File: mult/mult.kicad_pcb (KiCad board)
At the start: 2 copper layers, 20 x 108 mm, 73 parts, among them J1 Eurorack_Power, J10 Eurorack_Mono_Jack, J11 Eurorack_Mono_Jack, J12 Eurorack_Mono_Jack_No_S, J13 Eurorack_Mono_Jack_No_S, J14 Eurorack_Mono_Jack, J15 Eurorack_Mono_Jack, J16 Eurorack_Mono_Jack_No_S, J17 Eurorack_Mono_Jack_No_S, J2 Eurorack_Mono_Jack, J3 Eurorack_Mono_Jack, J4 Eurorack_Mono_Jack_No_S, J5 Eurorack_Mono_Jack_No_S, J6 Eurorack_Mono_Jack, J7 Eurorack_Mono_Jack, J8 Eurorack_Mono_Jack_No_S, J9 Eurorack_Mono_Jack_No_S, U1 OPA4197xPW, U2 OPA4197xPW, U3 OPA4197xPW, U4 OPA4197xPW

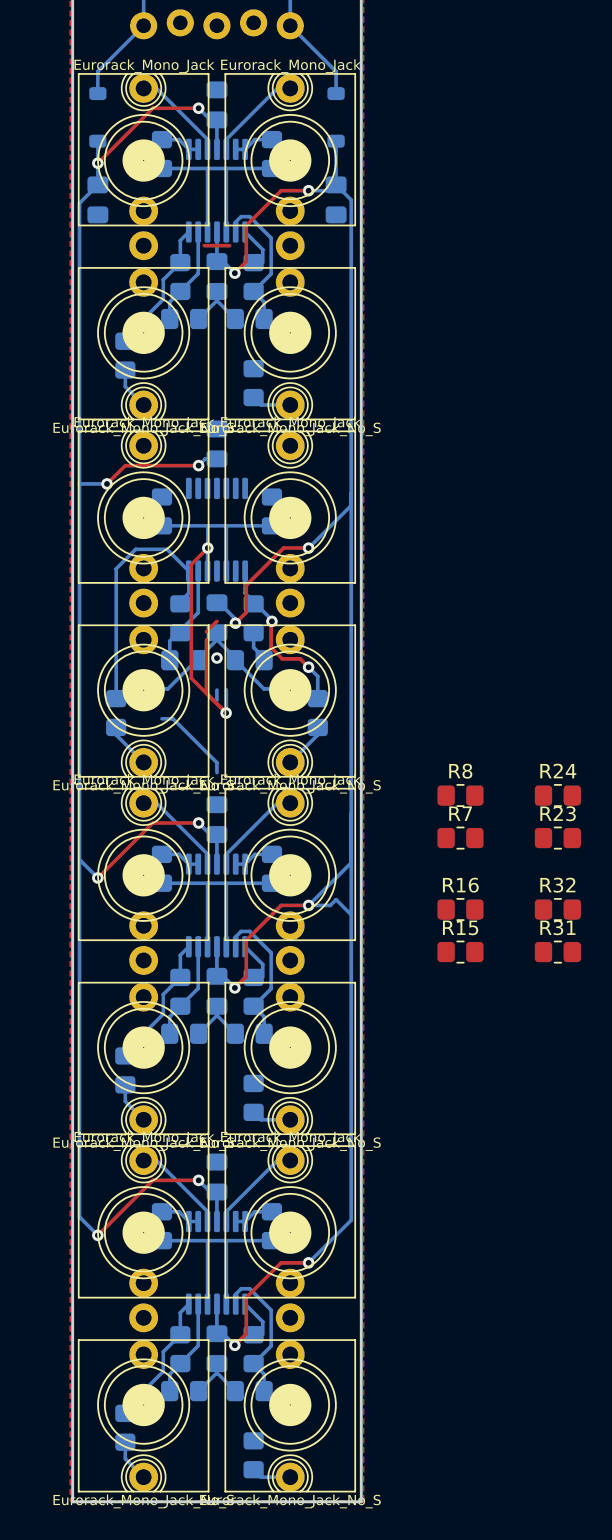
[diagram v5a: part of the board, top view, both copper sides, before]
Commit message: mult: Initial board routed, all items connected
Still expecting to make major changes this looks like mostly-random item
placements.
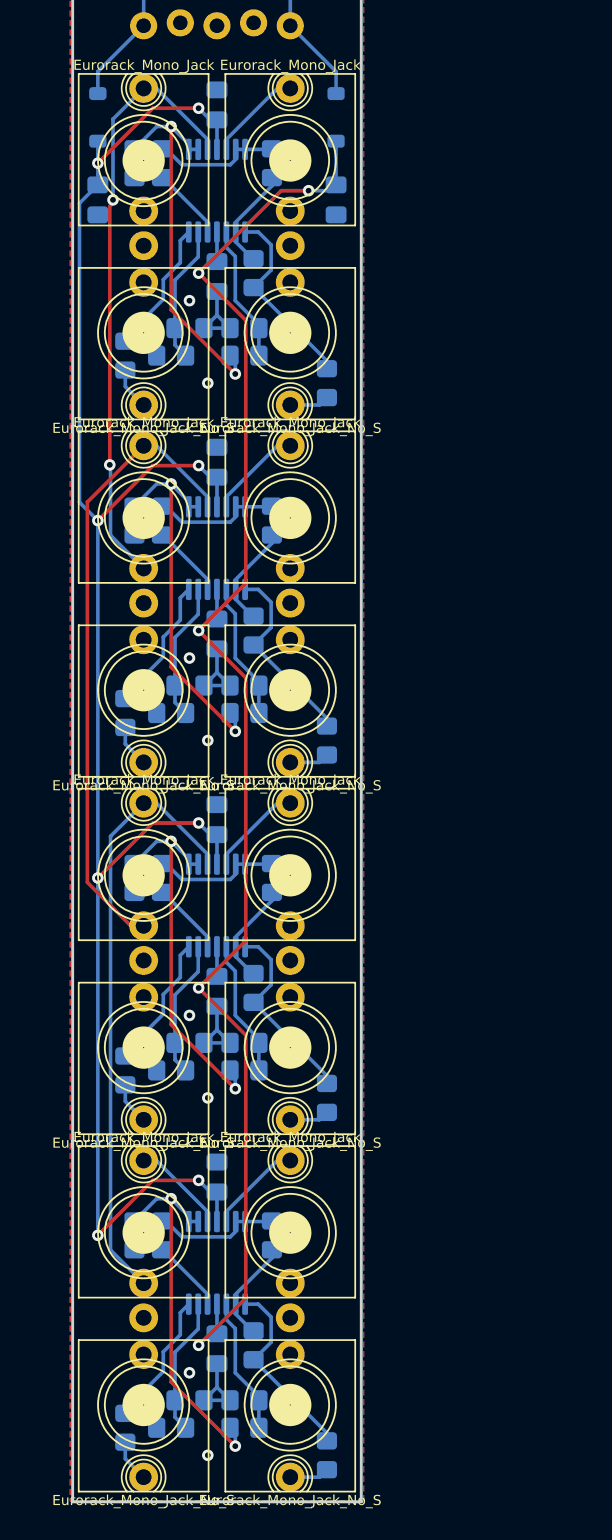
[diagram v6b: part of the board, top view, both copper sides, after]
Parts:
- R15, R16, R23, R24, R31, R32, R7, R8: moved to B.Cu
- moved R7 48.6 mm to (14.0, 15.2), turned to 90 degrees
- moved R8 38.9 mm to (12.7, 22.9), turned to -90 degrees
- moved R32 36.8 mm to (12.7, 97.2), turned to -90 degrees
- moved R15 32.6 mm to (14.0, 40.0), turned to 90 degrees
- moved R31 27.9 mm to (14.0, 89.5), turned to 90 degrees
- moved R24 24.9 mm to (12.7, 72.4), turned to -90 degrees
- moved R16 24.1 mm to (12.7, 47.6), turned to -90 degrees
- moved R23 20.0 mm to (14.0, 64.8), turned to 90 degrees
- moved R10 7.65 mm to (6.35, 40.0), turned to -90 degrees
- moved R18 7.65 mm to (6.35, 64.8), turned to -90 degrees
- moved R2 7.65 mm to (6.35, 15.2), turned to -90 degrees
- moved R26 7.65 mm to (6.35, 89.5), turned to -90 degrees
- moved R11 6.60 mm to (6.99, 53.3), turned to 180 degrees
- moved R13 6.60 mm to (12.1, 53.3), turned to 180 degrees
- moved R19 5.48 mm to (6.99, 78.1), turned to 180 degrees
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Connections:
- R13 pad 2: Net-(U2B--) -> Net-(U2A--)
- R15 pad 2: Net-(U2A--) -> Net-(U2B--)
- R21 pad 2: Net-(U3B--) -> Net-(U3A--)
- R23 pad 2: Net-(U3A--) -> Net-(U3B--)
- R29 pad 2: Net-(U4B--) -> Net-(U4A--)
- R31 pad 2: Net-(U4A--) -> Net-(U4B--)
- R5 pad 2: Net-(U1B--) -> Net-(U1A--)
- R7 pad 2: Net-(U1A--) -> Net-(U1B--)
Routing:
- net (no net): track 86.1 -> 0.00 mm
- net /channel 2/tip in (a): track 0.00 -> 43.6 mm
- net VEE: track 149.0 -> 109.0 mm, vias 8 -> 5
- net /channel 1/tip in (a): track 6.58 -> 42.1 mm, vias 0 -> 2
- net /channel 3/tip in (a): track 6.58 -> 41.8 mm
- net Net-(U2A--): track 0.00 -> 25.5 mm, vias 0 -> 2
- net Net-(U3A--): track 2.79 -> 25.5 mm, vias 0 -> 2
- net Net-(U1A--): track 2.79 -> 25.5 mm, vias 0 -> 2
- net Net-(U4A--): track 2.79 -> 25.5 mm, vias 0 -> 2
- net Net-(R32-Pad2): track 0.00 -> 13.4 mm
- net Net-(R24-Pad2): track 0.00 -> 13.4 mm
- net Net-(R34-Pad1): track 0.00 -> 13.4 mm
- net Net-(R16-Pad2): track 0.00 -> 13.4 mm
- net Net-(U3C-+): track 0.00 -> 9.23 mm
- net Net-(U4C-+): track 0.00 -> 9.23 mm
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
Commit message: mult: Replace OPA4917 with OPA1697
This seems reasonable performance (2mV offset max, audio op amp etc) and
significantly lower cost.
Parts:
- U1, U2, U3, U4: value OPA4197xPW -> OPA1679
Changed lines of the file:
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@@
     (property "Sheetfile" "channel.kicad_sch")
     (property "Sheetname" "channel 4")
-    (property "ki_description" "Quad 36V, Precision, Rail-to-Rail Input/Output, Low Offset Voltage, Operational Amplifier, TSSOP-14")
-    (property "ki_keywords" "quad opamp rtor")
+    (property "ki_description" "Low-Distortion Audio Operational Amplifiers, SOIC-14/TSSOP-14")
+    (property "ki_keywords" "quad opamp")
     (attr smd)
     (fp_text reference "U4" (at 0 3.45 90) (layer "B.SilkS")
         (effects (font (size 1 1) (thickness 0.15)) (justify mirror))
     )
-    (fp_text value "OPA4197xPW" (at 0 -3.45 90) (layer "B.Fab")
+    (fp_text value "OPA1679" (at 0 -3.45 90) (layer "B.Fab")
         (effects (font (size 1 1) (thickness 0.15)) (justify mirror))
     )
@@
     (property "Sheetfile" "channel.kicad_sch")
     (property "Sheetname" "channel 1")
-    (property "ki_description" "Quad 36V, Precision, Rail-to-Rail Input/Output, Low Offset Voltage, Operational Amplifier, TSSOP-14")
-    (property "ki_keywords" "quad opamp rtor")
+    (property "ki_description" "Low-Distortion Audio Operational Amplifiers, SOIC-14/TSSOP-14")
+    (property "ki_keywords" "quad opamp")
     (attr smd)
     (fp_text reference "U1" (at 0 3.45 90) (layer "B.SilkS")
         (effects (font (size 1 1) (thickness 0.15)) (justify mirror))
     )
-    (fp_text value "OPA4197xPW" (at 0 -3.45 90) (layer "B.Fab")
+    (fp_text value "OPA1679" (at 0 -3.45 90) (layer "B.Fab")
         (effects (font (size 1 1) (thickness 0.15)) (justify mirror))
     )
@@
     (property "Sheetfile" "channel.kicad_sch")
     (property "Sheetname" "channel 2")
-    (property "ki_description" "Quad 36V, Precision, Rail-to-Rail Input/Output, Low Offset Voltage, Operational Amplifier, TSSOP-14")
-    (property "ki_keywords" "quad opamp rtor")
+    (property "ki_description" "Low-Distortion Audio Operational Amplifiers, SOIC-14/TSSOP-14")
+    (property "ki_keywords" "quad opamp")
     (attr smd)
     (fp_text reference "U2" (at 0 3.45 90) (layer "B.SilkS")
         (effects (font (size 1 1) (thickness 0.15)) (justify mirror))
     )
-    (fp_text value "OPA4197xPW" (at 0 -3.45 90) (layer "B.Fab")
+    (fp_text value "OPA1679" (at 0 -3.45 90) (layer "B.Fab")
         (effects (font (size 1 1) (thickness 0.15)) (justify mirror))
     )
@@
     (property "Sheetfile" "channel.kicad_sch")
     (property "Sheetname" "channel 3")
-    (property "ki_description" "Quad 36V, Precision, Rail-to-Rail Input/Output, Low Offset Voltage, Operational Amplifier, TSSOP-14")
-    (property "ki_keywords" "quad opamp rtor")
+    (property "ki_description" "Low-Distortion Audio Operational Amplifiers, SOIC-14/TSSOP-14")
+    (property "ki_keywords" "quad opamp")
     (attr smd)
     (fp_text reference "U3" (at 0 3.45 90) (layer "B.SilkS")
         (effects (font (size 1 1) (thickness 0.15)) (justify mirror))
     )
-    (fp_text value "OPA4197xPW" (at 0 -3.45 90) (layer "B.Fab")
-        (effects (font (size 1 1) (thickness 0.15)) (justify mirror))
-    )
+    (fp_text value "OPA1679" (at 0 -3.45 90) (layer "B.Fab")
+        (effects (font (size 1 1) (thickness 0.15)) (justify mirror))
+    )

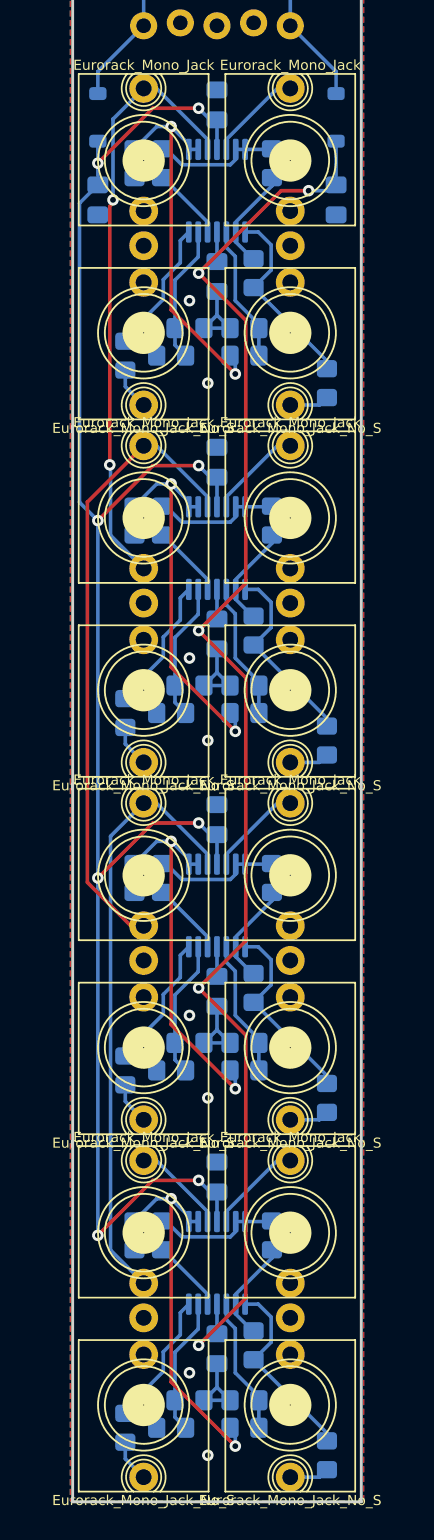
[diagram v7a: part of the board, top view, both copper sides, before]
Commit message: mult: Progress rerouting easier layout
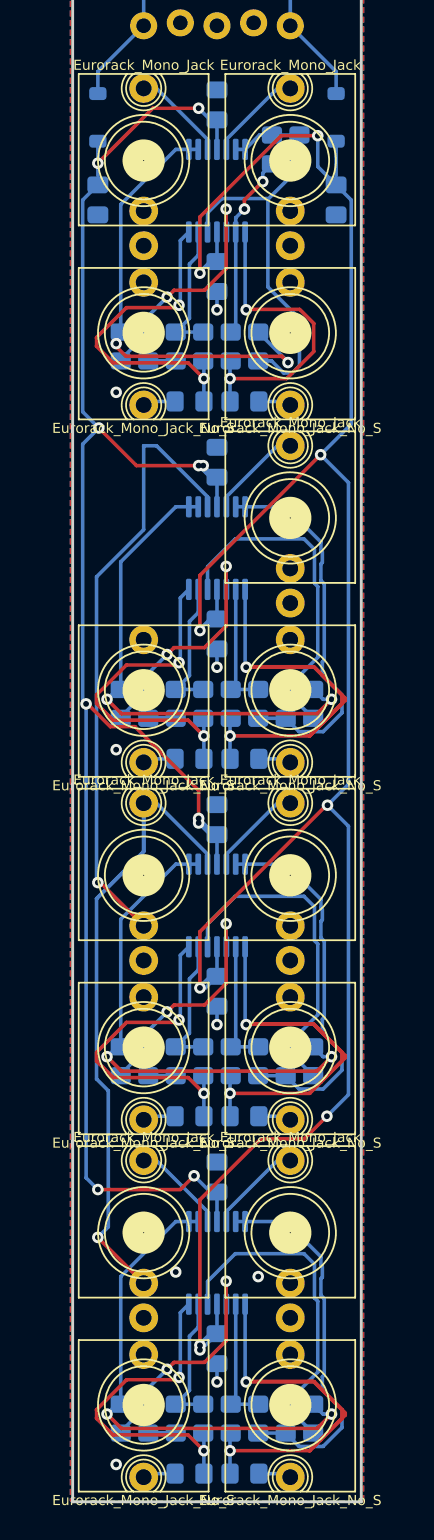
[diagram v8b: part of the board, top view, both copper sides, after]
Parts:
- removed the J6 at (5.08, 39.8)
- moved R21 17.7 mm to (16.8, 77.5)
- moved R31 17.7 mm to (16.8, 102.2)
- moved R11 17.7 mm to (16.8, 52.7)
- moved R22 15.3 mm to (14.9, 77.5), turned to 90 degrees
- moved R32 15.3 mm to (14.9, 102.2), turned to 90 degrees
- moved R1 15.3 mm to (13.0, 27.9)
- moved R12 15.3 mm to (14.9, 52.7), turned to 90 degrees
- moved R23 12.7 mm to (13.0, 77.5), turned to -90 degrees
- moved R33 12.7 mm to (13.0, 102.2), turned to -90 degrees
- moved R13 12.7 mm to (13.0, 52.7), turned to -90 degrees
- moved R2 9.57 mm to (15.9, 14.3)
- moved R14 8.60 mm to (3.49, 52.7), turned to 90 degrees
- moved R24 8.60 mm to (3.49, 77.5), turned to 90 degrees
- moved R34 8.60 mm to (3.49, 102.2), turned to 90 degrees
- moved R4 8.60 mm to (3.49, 27.9), turned to 90 degrees
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- renumbered C3 to C1, C2 to C10, C4 to C2, C5 to C3, C6 to C4, C7 to C5, C8 to C6, C9 to C7, C10 to C8, C1 to C9, J2 to J1, J11 to J10, J12 to J11, J13 to J12, J14 to J13, J15 to J14, J16 to J15, J17 to J16, J1 to J17, J3 to J2, J4 to J3, J5 to J4, J7 to J6, J8 to J7, J9 to J8, J10 to J9, R4 to R10, R9 to R11, R10 to R12, R15 to R13, R13 to R14, R35 to R15, R36 to R16, R11 to R17, R14 to R18, R16 to R19, R12 to R20, R17 to R21, R18 to R22, R21 to R24, R37 to R25, R38 to R26, R19 to R27, R22 to R28, R24 to R29, R7 to R3, R20 to R30, R25 to R31, R26 to R32, R31 to R33, R29 to R34, R39 to R35, R40 to R36, R27 to R37, R30 to R38, R32 to R39, R5 to R4, R28 to R40, R33 to R5, R34 to R6, R3 to R7, R6 to R8, R8 to R9
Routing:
- net VEE: track 109.0 -> 158.8 mm, vias 5 -> 9
- net /channel 1/tip in (a): track 42.1 -> 6.58 mm, vias 2 -> 0
- net Net-(R16-Pad1): track 13.4 -> 36.4 mm, vias 0 -> 2
- net Net-(R26-Pad1): track 13.4 -> 36.4 mm, vias 0 -> 2
- net Net-(R36-Pad1): track 13.4 -> 36.4 mm, vias 0 -> 2
- net Net-(U1D-+): track 6.95 -> 25.2 mm
- net Net-(U2B--): track 8.61 -> 26.3 mm
- net Net-(U4B--): track 8.61 -> 26.3 mm
- net Net-(U3B--): track 8.61 -> 26.3 mm
- net Net-(U2D-+): track 6.95 -> 23.5 mm
- net Net-(U4D-+): track 6.95 -> 23.5 mm
- net Net-(U3D-+): track 6.95 -> 23.5 mm
- net Net-(R35-Pad1): track 11.7 -> 23.8 mm, vias 0 -> 2
- net Net-(R25-Pad1): track 11.7 -> 23.8 mm, vias 0 -> 2
- net Net-(R5-Pad1): track 11.7 -> 23.8 mm, vias 0 -> 2
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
